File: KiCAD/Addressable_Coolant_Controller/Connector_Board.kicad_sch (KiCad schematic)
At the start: 0 parts

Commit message: Fixed broken netclasses, removed voltage divider circuit
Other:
- company: (none) -> Warner Consulting Inc.
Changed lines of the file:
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@@
 (kicad_sch (version 20230121) (generator eeschema)
   (paper "A4")
+  (title_block
+    (company "Warner Consulting Inc.")
+  )
 )

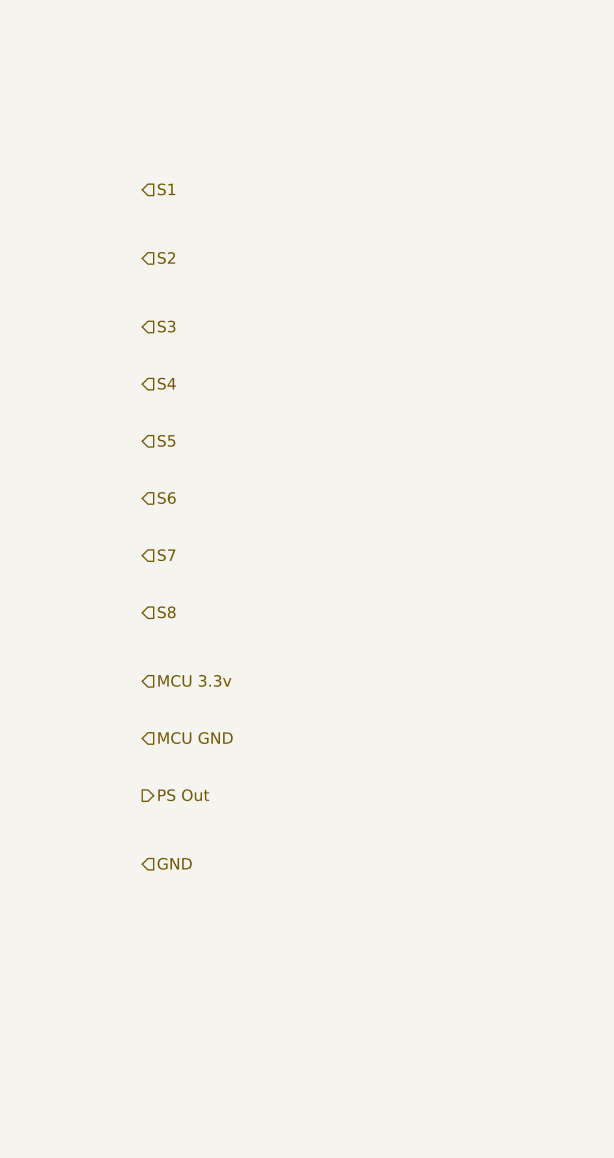
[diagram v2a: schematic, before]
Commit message: Added second board outline and circular connectors
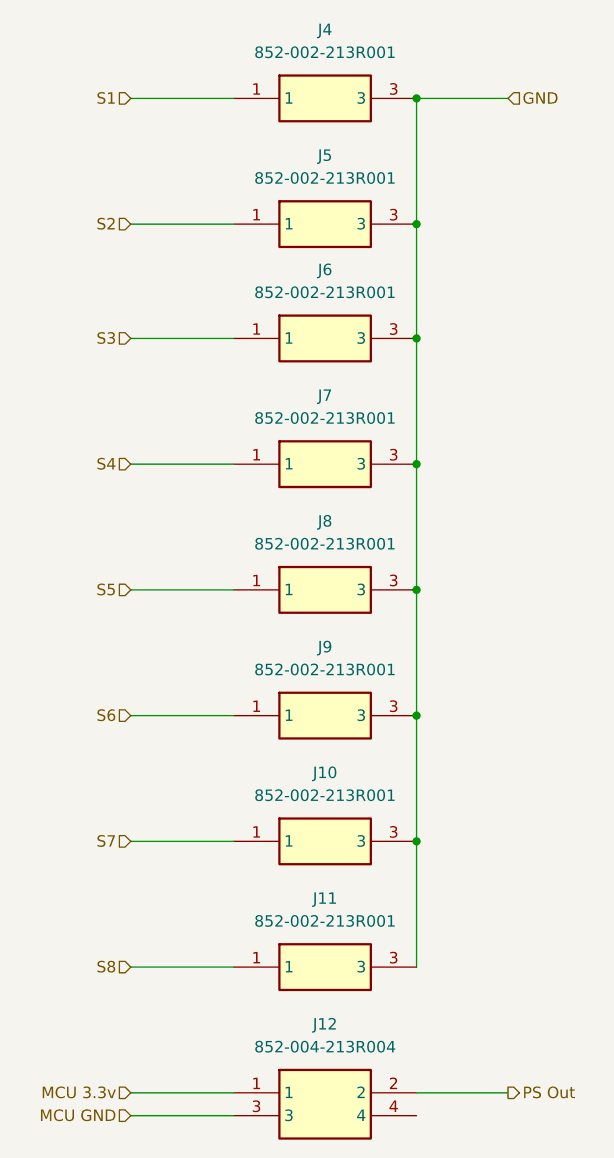
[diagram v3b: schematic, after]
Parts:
- added J10, J11, J4, J5, J6, J7, J8, J9: 852-002-213R001, 852-002-213R001:852-002-213R001, symbol 852-002-213R001:852-002-213R001
- added J12: 852-004-213R004, 852-002-213R004:852004213R004, symbol 852-004-213R004:852-004-213R004
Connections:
- net GND: now also J10.3, J11.3, J4.3, J5.3, J6.3, J7.3, J8.3, J9.3
- net MCU 3.3v: now also J12.1
- net MCU GND: now also J12.3
- net PS Out: now also J12.2
- net S1: now also J4.1
- net S2: now also J5.1
- net S3: now also J6.1
- net S4: now also J7.1
- net S5: now also J8.1
- net S6: now also J9.1
- net S7: now also J10.1
- net S8: now also J11.1

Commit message: Routed connector PCB and fixed components designators
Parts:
- renumbered J4 to J1, J5 to J2, J6 to J3, J7 to J4, J8 to J5, J9 to J6, J10 to J7, J11 to J8, J12 to J9

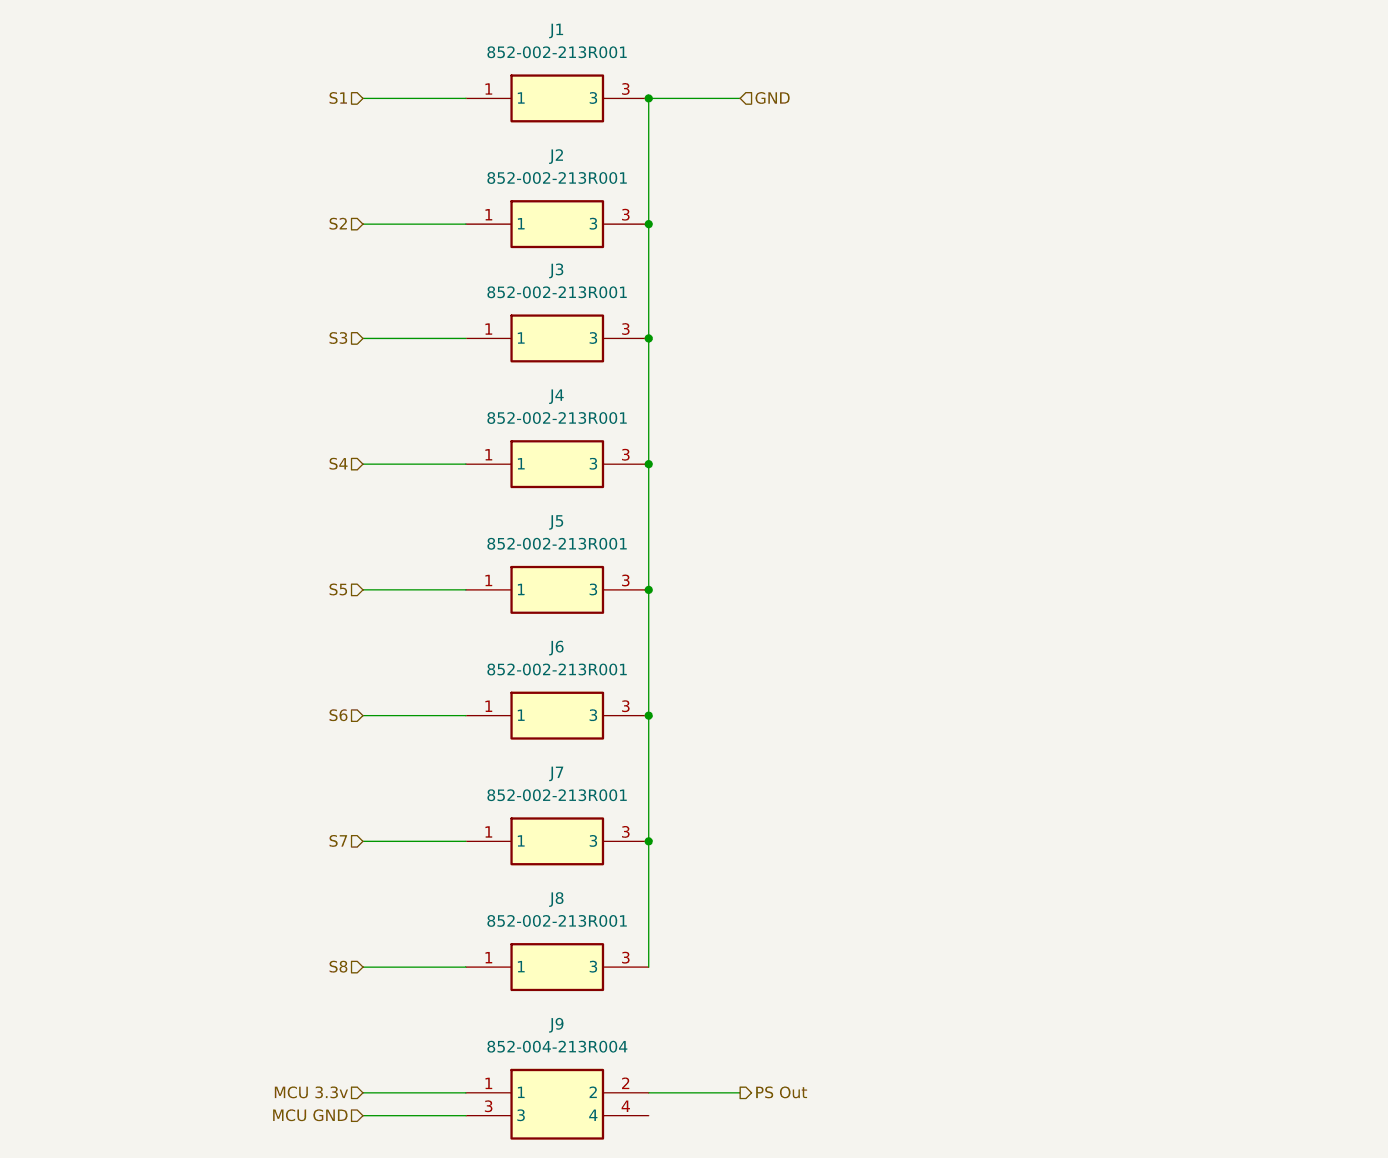
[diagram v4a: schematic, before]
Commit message: Added LEDs to connector board, and moved to hierarchical sheet
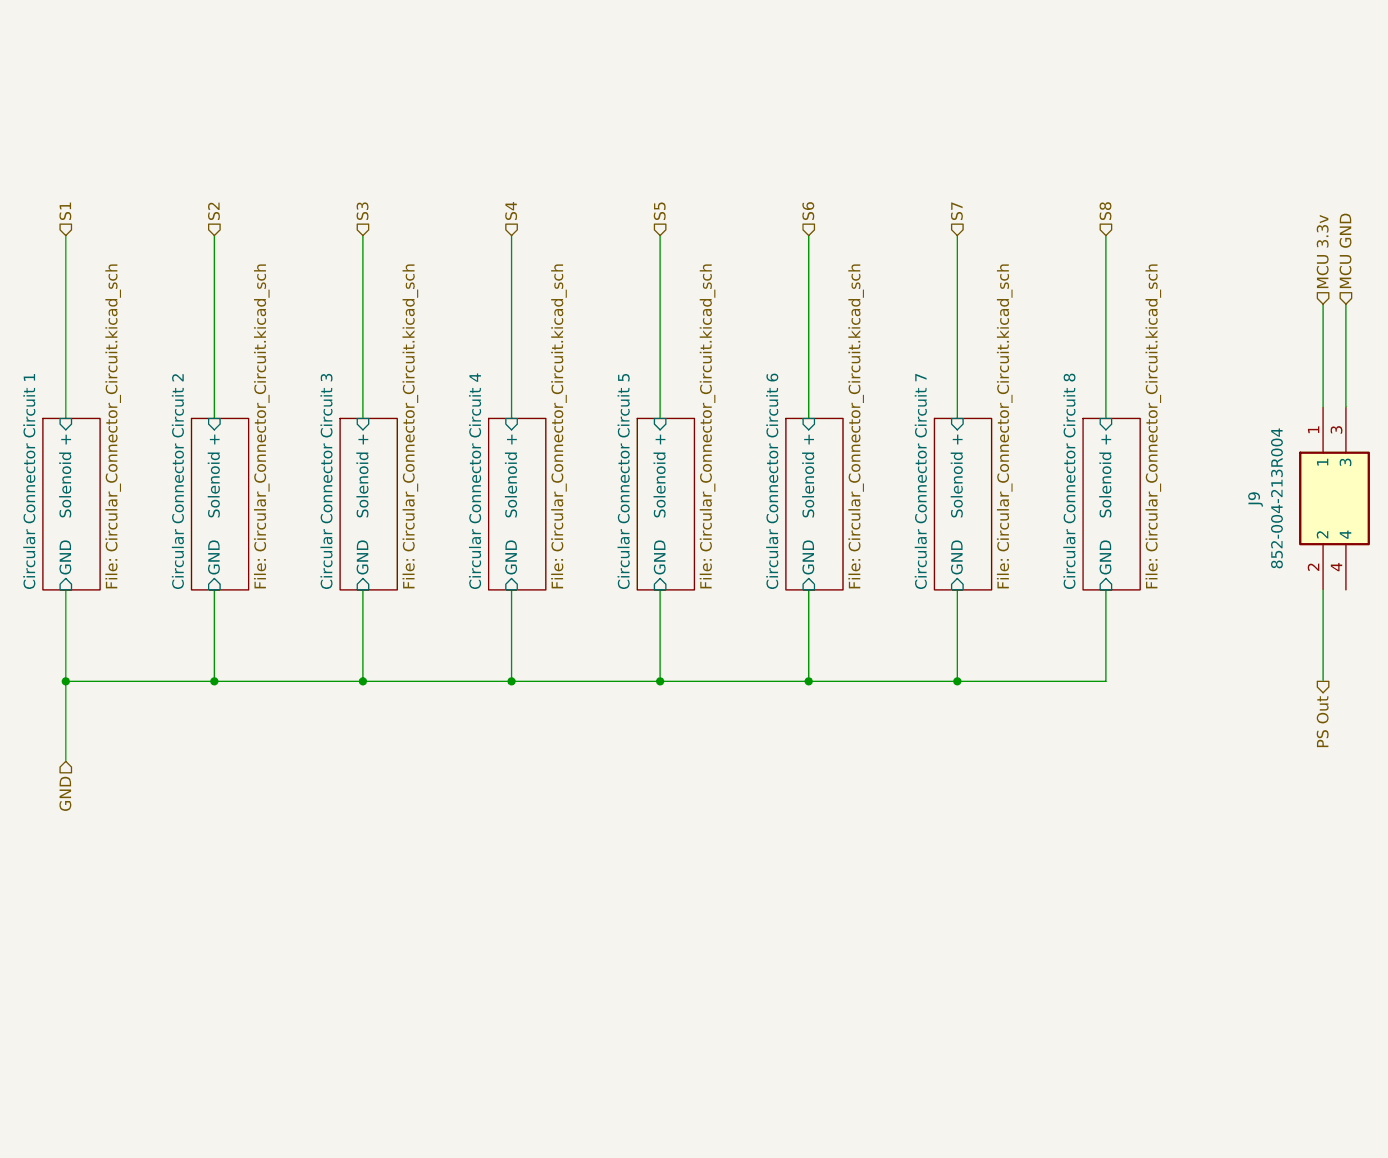
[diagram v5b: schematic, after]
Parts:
- removed J1, J2, J3, J4, J5, J6, J7, J8: 852-002-213R001, 852-002-213R001:852-002-213R001, symbol 852-002-213R001:852-002-213R001
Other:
- added sheet Circular Connector Circuit 1 (Circular_Connector_Circuit.kicad_sch)
- added sheet Circular Connector Circuit 2 (Circular_Connector_Circuit.kicad_sch)
- added sheet Circular Connector Circuit 3 (Circular_Connector_Circuit.kicad_sch)
- added sheet Circular Connector Circuit 4 (Circular_Connector_Circuit.kicad_sch)
- added sheet Circular Connector Circuit 5 (Circular_Connector_Circuit.kicad_sch)
- added sheet Circular Connector Circuit 6 (Circular_Connector_Circuit.kicad_sch)
- added sheet Circular Connector Circuit 7 (Circular_Connector_Circuit.kicad_sch)
- added sheet Circular Connector Circuit 8 (Circular_Connector_Circuit.kicad_sch)
- moved on the sheet: J9
